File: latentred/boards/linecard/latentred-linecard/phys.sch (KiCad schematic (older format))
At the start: 0 parts

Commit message: Continued work on line card design. Now have PSU and all PHYs, still working on clock distribution.
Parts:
- added C100, C101, C105, C106, C107, C108, C109, C110, C111, C112, C113, C117, C118, C119, C123, C124, C125, C145, C149, C153, C157, C16, C161, C162, C163, C164, C177, C178, C179, C180, C185, C186, C187, C188, C189, C190, C191, C192, C193, C194, C195, C196, C20, C201, C202, C203, C204, C205, C206, C207, C208, C209, C210, C211, C212, C217, C218, C219, C220, C225, C226, C227, C228, C233, C24, C25, C26, C27, C28, C29, C30, C31, C32, C63, C67, C71, C75, C76, C77, C87, C88, C89, C93, C94, C95, C96, C97, C98, C99: 0.47 uF, symbol device:C
- added C102, C103, C104, C114, C115, C116, C12, C120, C121, C122, C129, C13, C130, C131, C132, C133, C134, C135, C136, C137, C138, C139, C14, C140, C141, C142, C143, C144, C15, C181, C182, C183, C184, C197, C198, C199, C200, C213, C214, C215, C216, C221, C222, C223, C224, C46, C47, C48, C49, C51, C52, C53, C54, C55, C56, C57, C58, C59, C60, C61, C62, C90, C91, C92: 0.1 uF, symbol device:C
- added C126, C127, C128, C229, C230, C231, C232, C50: 10 nF 2 kV, symbol device:C
- added C146, C147, C148, C150, C151, C152, C154, C155, C156, C158, C159, C160, C165, C166, C167, C168, C169, C17, C170, C171, C172, C173, C174, C175, C176, C18, C19, C21, C22, C23, C64, C65, C66, C68, C69, C70, C72, C73, C74, C78, C79, C80, C81, C82, C83, C84, C85, C86: 4.7 uF, symbol device:C
- added J2: STEWART_SS_74500_024, symbol special-azonenberg:STEWART_SS_74500_024
- added L10, L11, L12, L13, L14, L15, L16, L20, L21, L22, L23, L24, L25, L26, L27, L28, L29, L30, L31, L4, L5, L6, L8, L9: 600R, symbol passive-azonenberg:INDUCTOR_PWROUT
- added L17, L18, L19, L32, L33, L34, L35, L7: BOURNS_PT6120EL, symbol special-azonenberg:BOURNS_PT6120EL
- added Q1, Q2, Q3, Q4, Q5, Q6, Q7, Q8: SSM6N58NU, symbol special-azonenberg:SSM6N58NU_DUAL_NMOS
- added R100, R101, R102, R103, R104, R105, R106, R107, R108, R109, R110, R132, R134, R136, R138, R23, R26, R44, R45, R46, R47, R48, R49, R66, R68, R70, R94, R97, R98, R99: 2.49K, symbol device:R
- added R111, R112, R113, R114, R115, R116, R117, R118, R119, R121, R123, R125, R127, R128, R129, R130, R29, R30, R31, R32, R50, R51, R52, R53, R54, R55, R56, R58, R60, R62, R63, R64: 75, symbol device:R
- added R120, R122, R124, R126, R139, R140, R141, R142, R24, R27, R57, R59, R61, R71, R72, R73: 470, symbol device:R
- added R131, R133, R135, R137, R25, R40, R65, R67, R69, R86: 10K, symbol device:R
- added R143: 33, symbol device:R
- added R20, R33, R35, R37, R74, R76, R78, R80: 11K, symbol device:R
- added R21, R34, R36, R38, R75, R77, R79, R81, R83, R84, R87, R88, R91, R92, R95, R96: 10k, symbol device:R
- added R22, R39, R41, R43, R82, R85, R89, R93: 5.76K, symbol device:R
- added R28: 2.0K, symbol device:R
- added R42, R90: 5.76k, symbol device:R
- added U10, U11, U12, U13, U14, U15, U8, U9: DP83867, symbol special-azonenberg:DP83867
- added U16: DSC6101CI2A-025.0000, symbol osc-azonenberg:OSC
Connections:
- new net: R20.2, U8.12 (RBIAS)
- new net: C12.1, U8.27 (TX_D1/SGMII_TX_P)
- new net: C13.1, U8.28 (TX_D0/SGMII_TX_N)
- new net: C14.1, U8.35 (RX_D2/SGMII_RX_P)
- new net: C15.1, U8.36 (RX_D3/SGMII_RX_N)
- new net: R21.2, U8.44 (~INT~/~PWRDN~)
- new net: Q1.D1 (D), R24.2
- new net: Q1.D2 (D), R27.2
- new net: C49.2, L7.1 (A_CT)
- new net: C46.2, L7.10 (D_CT)
- new net: L7.15 (DM_CT), R32.2
- new net: L7.18 (CM_CT), R31.2
- new net: L7.21 (BM_CT), R30.2
- new net: L7.24 (AM_CT), R29.2
- new net: C48.2, L7.4 (B_CT)
- new net: C47.2, L7.7 (C_CT)
- new net: C50.2, R29.1, R30.1, R31.1, R32.1
- new net: R33.2, U9.12 (RBIAS)
- new net: C51.1, U9.27 (TX_D1/SGMII_TX_P)
- new net: C52.1, U9.28 (TX_D0/SGMII_TX_N)
- new net: C53.1, U9.35 (RX_D2/SGMII_RX_P)
- new net: C54.1, U9.36 (RX_D3/SGMII_RX_N)
- new net: R34.2, U9.44 (~INT~/~PWRDN~)
- new net: Q2.D1 (D), R57.2
- new net: Q3.D2 (D), R71.2
- new net: C120.2, L17.1 (A_CT)
- new net: C90.2, L17.10 (D_CT)
- new net: L17.15 (DM_CT), R62.2
- new net: L17.18 (CM_CT), R56.2
- new net: L17.21 (BM_CT), R53.2
- new net: L17.24 (AM_CT), R50.2
- new net: C114.2, L17.4 (B_CT)
- new net: C102.2, L17.7 (C_CT)
- new net: C126.2, R50.1, R53.1, R56.1, R62.1
- new net: R35.2, U10.12 (RBIAS)
- new net: C55.1, U10.27 (TX_D1/SGMII_TX_P)
- new net: C56.1, U10.28 (TX_D0/SGMII_TX_N)
- new net: C57.1, U10.35 (RX_D2/SGMII_RX_P)
- new net: C58.1, U10.36 (RX_D3/SGMII_RX_N)
- new net: R36.2, U10.44 (~INT~/~PWRDN~)
- new net: Q2.D2 (D), R59.2
- new net: Q4.D1 (D), R72.2
- new net: C121.2, L18.1 (A_CT)
- new net: C91.2, L18.10 (D_CT)
- new net: L18.15 (DM_CT), R63.2
- new net: L18.18 (CM_CT), R58.2
- new net: L18.21 (BM_CT), R54.2
- new net: L18.24 (AM_CT), R51.2
- new net: C115.2, L18.4 (B_CT)
- new net: C103.2, L18.7 (C_CT)
- new net: C127.2, R51.1, R54.1, R58.1, R63.1
- new net: R37.2, U11.12 (RBIAS)
- new net: C59.1, U11.27 (TX_D1/SGMII_TX_P)
- new net: C60.1, U11.28 (TX_D0/SGMII_TX_N)
- new net: C61.1, U11.35 (RX_D2/SGMII_RX_P)
- new net: C62.1, U11.36 (RX_D3/SGMII_RX_N)
- new net: R38.2, U11.44 (~INT~/~PWRDN~)
- new net: Q3.D1 (D), R61.2
- new net: Q4.D2 (D), R73.2
- new net: C122.2, L19.1 (A_CT)
- new net: C92.2, L19.10 (D_CT)
- new net: L19.15 (DM_CT), R64.2
- new net: L19.18 (CM_CT), R60.2
- new net: L19.21 (BM_CT), R55.2
- new net: L19.24 (AM_CT), R52.2
- new net: C116.2, L19.4 (B_CT)
- new net: C104.2, L19.7 (C_CT)
- new net: C128.2, R52.1, R55.1, R60.1, R64.1
- new net: R74.2, U12.12 (RBIAS)
- new net: C129.1, U12.27 (TX_D1/SGMII_TX_P)
- new net: C130.1, U12.28 (TX_D0/SGMII_TX_N)
- new net: R75.2, U12.44 (~INT~/~PWRDN~)
- new net: Q5.D1 (D), R120.2
- new net: Q7.D1 (D), R139.2
- new net: C221.2, L32.1 (A_CT)
- new net: C181.2, L32.10 (D_CT)
- new net: L32.15 (DM_CT), R127.2
- new net: L32.18 (CM_CT), R119.2
- new net: L32.21 (BM_CT), R115.2
- new net: L32.24 (AM_CT), R111.2
- new net: C213.2, L32.4 (B_CT)
- new net: C197.2, L32.7 (C_CT)
- new net: C229.2, R111.1, R115.1, R119.1, R127.1
- new net: R76.2, U13.12 (RBIAS)
- new net: C133.1, U13.27 (TX_D1/SGMII_TX_P)
- new net: C134.1, U13.28 (TX_D0/SGMII_TX_N)
- new net: R77.2, U13.44 (~INT~/~PWRDN~)
- new net: Q5.D2 (D), R122.2
- new net: Q7.D2 (D), R140.2
- new net: C222.2, L33.1 (A_CT)
- new net: C182.2, L33.10 (D_CT)
- new net: L33.15 (DM_CT), R128.2
- new net: L33.18 (CM_CT), R121.2
- new net: L33.21 (BM_CT), R116.2
- new net: L33.24 (AM_CT), R112.2
- new net: C214.2, L33.4 (B_CT)
- new net: C198.2, L33.7 (C_CT)
- new net: C230.2, R112.1, R116.1, R121.1, R128.1
- new net: R78.2, U14.12 (RBIAS)
- new net: C137.1, U14.27 (TX_D1/SGMII_TX_P)
- new net: C138.1, U14.28 (TX_D0/SGMII_TX_N)
- new net: R79.2, U14.44 (~INT~/~PWRDN~)
- new net: Q6.D1 (D), R124.2
- new net: Q8.D1 (D), R141.2
- new net: C223.2, L34.1 (A_CT)
- new net: C183.2, L34.10 (D_CT)
- new net: L34.15 (DM_CT), R129.2
- new net: L34.18 (CM_CT), R123.2
- new net: L34.21 (BM_CT), R117.2
- new net: L34.24 (AM_CT), R113.2
- new net: C215.2, L34.4 (B_CT)
- new net: C199.2, L34.7 (C_CT)
- new net: C231.2, R113.1, R117.1, R123.1, R129.1
- new net: R80.2, U15.12 (RBIAS)
- new net: C141.1, U15.27 (TX_D1/SGMII_TX_P)
- new net: C142.1, U15.28 (TX_D0/SGMII_TX_N)
- new net: R81.2, U15.44 (~INT~/~PWRDN~)
- new net: Q6.D2 (D), R126.2
- new net: Q8.D2 (D), R142.2
- new net: C224.2, L35.1 (A_CT)
- new net: C184.2, L35.10 (D_CT)
- new net: L35.15 (DM_CT), R130.2
- new net: L35.18 (CM_CT), R125.2
- new net: L35.21 (BM_CT), R118.2
- new net: L35.24 (AM_CT), R114.2
- new net: C216.2, L35.4 (B_CT)
- new net: C200.2, L35.7 (C_CT)
- new net: C232.2, R114.1, R118.1, R125.1, R130.1
- new net: R143.2, U16.3 (CLK)
- new net 1V0: C148.1, C152.1, C156.1, C160.1, C19.1, C66.1, C70.1, C74.1, L10.2, L13.2, L16.2, L22.2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
- new net 1V8: C145.1, C147.1, C149.1, C151.1, C153.1, C155.1, C157.1, C159.1, C16.1, C161.1, C162.1, C163.1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
- new net 2V5: C146.1, C150.1, C154.1, C158.1, C17.1, C64.1, C68.1, C72.1, L11.2, L14.2, L20.2, L23.2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
- new net 3V3: J2.A11 (YELLOW_LED_P), J2.A9 (GREEN_LED_P), J2.B11 (YELLOW_LED_P), J2.B9 (GREEN_LED_P), J2.C11 (YELLOW_LED_P), J2.C9 (GREEN_LED_P), J2.D11 (YELLOW_LED_P), J2.D9 (GREEN_LED_P), J2.E11 (YELLOW_LED_P), J2.E9 (GREEN_LED_P), J2.F11 (YELLOW_LED_P), J2.F9 (GREEN_LED_P)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
- new net A1V0_0: C23.1, C27.1, C30.1, C31.1, C32.1, L6.1, U8.24 (1V0), U8.31 (1V0), U8.42 (1V0), U8.6 (1V0)
- new net A1V0_1: C107.1, C117.1, C123.1, C80.1, C95.1, L10.1, U9.24 (1V0), U9.31 (1V0), U9.42 (1V0), U9.6 (1V0)
- new net A1V0_2: C110.1, C118.1, C124.1, C83.1, C98.1, L13.1, U10.24 (1V0), U10.31 (1V0), U10.42 (1V0), U10.6 (1V0)
- new net A1V0_3: C101.1, C113.1, C119.1, C125.1, C86.1, L16.1, U11.24 (1V0), U11.31 (1V0), U11.42 (1V0), U11.6 (1V0)
- new net A1V0_4: C167.1, C187.1, C203.1, C217.1, C225.1, L22.1, U12.24 (1V0), U12.31 (1V0), U12.42 (1V0), U12.6 (1V0)
- new net A1V0_5: C170.1, C190.1, C206.1, C218.1, C226.1, L25.1, U13.24 (1V0), U13.31 (1V0), U13.42 (1V0), U13.6 (1V0)
- new net A1V0_6: C173.1, C193.1, C209.1, C219.1, C227.1, L28.1, U14.24 (1V0), U14.31 (1V0), U14.42 (1V0), U14.6 (1V0)
- new net A1V0_7: C176.1, C196.1, C212.1, C220.1, C228.1, L31.1, U15.24 (1V0), U15.31 (1V0), U15.42 (1V0), U15.6 (1V0)
- new net A1V8_0: C22.1, C26.1, C29.1, L5.1, U8.13 (A1V8), U8.48 (A1V8)
- new net A1V8_1: C106.1, C79.1, C94.1, L9.1, U9.13 (A1V8), U9.48 (A1V8)
- new net A1V8_2: C109.1, C82.1, C97.1, L12.1, U10.13 (A1V8), U10.48 (A1V8)
- new net A1V8_3: C100.1, C112.1, C85.1, L15.1, U11.13 (A1V8), U11.48 (A1V8)
- new net A1V8_4: C166.1, C186.1, C202.1, L21.1, U12.13 (A1V8), U12.48 (A1V8)
- new net A1V8_5: C169.1, C189.1, C205.1, L24.1, U13.13 (A1V8), U13.48 (A1V8)
- new net A1V8_6: C172.1, C192.1, C208.1, L27.1, U14.13 (A1V8), U14.48 (A1V8)
- new net A1V8_7: C175.1, C195.1, C211.1, L30.1, U15.13 (A1V8), U15.48 (A1V8)
- new net A2V5_0: C21.1, C25.1, C28.1, L4.1, U8.3 (A2V5), U8.9 (A2V5)
- new net A2V5_1: C105.1, C78.1, C93.1, L8.1, U9.3 (A2V5), U9.9 (A2V5)
- new net A2V5_2: C108.1, C81.1, C96.1, L11.1, U10.3 (A2V5), U10.9 (A2V5)
- new net A2V5_3: C111.1, C84.1, C99.1, L14.1, U11.3 (A2V5), U11.9 (A2V5)
- new net A2V5_4: C165.1, C185.1, C201.1, L20.1, U12.3 (A2V5), U12.9 (A2V5)
- new net A2V5_5: C168.1, C188.1, C204.1, L23.1, U13.3 (A2V5), U13.9 (A2V5)
- new net A2V5_6: C171.1, C191.1, C207.1, L26.1, U14.3 (A2V5), U14.9 (A2V5)
- new net A2V5_7: C174.1, C194.1, C210.1, L29.1, U15.3 (A2V5), U15.9 (A2V5)
- new net CLK_25MHZ: R143.1
- new net CLK_25MHZ_0: U8.15 (XI)
- new net CLK_25MHZ_1: U9.15 (XI)
- new net CLK_25MHZ_2: U10.15 (XI)
- new net CLK_25MHZ_3: U11.15 (XI)
- new net CLK_25MHZ_4: U12.15 (XI)
- new net CLK_25MHZ_5: U13.15 (XI)
- new net CLK_25MHZ_6: U14.15 (XI)
- new net CLK_25MHZ_7: U15.15 (XI)
- new net ETH0_AM_N: J2.A2 (A_N), L7.22 (AM_N)
- new net ETH0_AM_P: J2.A1 (A_P), L7.23 (AM_P)
- new net ETH0_A_N: L7.3 (A_N), U8.2 (ETH_A_N)
- new net ETH0_A_P: L7.2 (A_P), U8.1 (ETH_A_P)
- new net ETH0_BM_N: J2.A4 (B_N), L7.19 (BM_N)
- new net ETH0_BM_P: J2.A3 (B_P), L7.20 (BM_P)
- new net ETH0_B_N: L7.6 (B_N), U8.5 (ETH_B_N)
- new net ETH0_B_P: L7.5 (B_P), U8.4 (ETH_B_P)
- new net ETH0_CM_N: J2.A6 (C_N), L7.16 (CM_N)
- new net ETH0_CM_P: J2.A5 (C_P), L7.17 (CM_P)
- new net ETH0_C_N: L7.9 (C_N), U8.8 (ETH_C_N)
- new net ETH0_C_P: L7.8 (C_P), U8.7 (ETH_C_P)
- new net ETH0_DM_N: J2.A8 (D_N), L7.13 (DM_N)
- new net ETH0_DM_P: J2.A7 (D_P), L7.14 (DM_P)
- new net ETH0_D_N: L7.12 (D_N), U8.11 (ETH_D_N)
- new net ETH0_D_P: L7.11 (D_P), U8.10 (ETH_D_P)
- new net ETH1_AM_N: J2.B2 (A_N), L17.22 (AM_N)
- new net ETH1_AM_P: J2.B1 (A_P), L17.23 (AM_P)
- new net ETH1_A_N: L17.3 (A_N), U9.2 (ETH_A_N)
- new net ETH1_A_P: L17.2 (A_P), U9.1 (ETH_A_P)
- new net ETH1_BM_N: J2.B4 (B_N), L17.19 (BM_N)
- new net ETH1_BM_P: J2.B3 (B_P), L17.20 (BM_P)
- new net ETH1_B_N: L17.6 (B_N), U9.5 (ETH_B_N)
- new net ETH1_B_P: L17.5 (B_P), U9.4 (ETH_B_P)
- new net ETH1_CM_N: J2.B6 (C_N), L17.16 (CM_N)
- new net ETH1_CM_P: J2.B5 (C_P), L17.17 (CM_P)
- new net ETH1_C_N: L17.9 (C_N), U9.8 (ETH_C_N)
- new net ETH1_C_P: L17.8 (C_P), U9.7 (ETH_C_P)
- new net ETH1_DM_N: J2.B8 (D_N), L17.13 (DM_N)
- new net ETH1_DM_P: J2.B7 (D_P), L17.14 (DM_P)
- new net ETH1_D_N: L17.12 (D_N), U9.11 (ETH_D_N)
- new net ETH1_D_P: L17.11 (D_P), U9.10 (ETH_D_P)
- new net ETH2_AM_N: J2.C2 (A_N), L18.22 (AM_N)
- new net ETH2_AM_P: J2.C1 (A_P), L18.23 (AM_P)
- new net ETH2_A_N: L18.3 (A_N), U10.2 (ETH_A_N)
- new net ETH2_A_P: L18.2 (A_P), U10.1 (ETH_A_P)
- new net ETH2_BM_N: J2.C4 (B_N), L18.19 (BM_N)
- new net ETH2_BM_P: J2.C3 (B_P), L18.20 (BM_P)
- new net ETH2_B_N: L18.6 (B_N), U10.5 (ETH_B_N)
- new net ETH2_B_P: L18.5 (B_P), U10.4 (ETH_B_P)
- new net ETH2_CM_N: J2.C6 (C_N), L18.16 (CM_N)
- new net ETH2_CM_P: J2.C5 (C_P), L18.17 (CM_P)
- new net ETH2_C_N: L18.9 (C_N), U10.8 (ETH_C_N)
- new net ETH2_C_P: L18.8 (C_P), U10.7 (ETH_C_P)
- new net ETH2_DM_N: J2.C8 (D_N), L18.13 (DM_N)
- new net ETH2_DM_P: J2.C7 (D_P), L18.14 (DM_P)
- new net ETH2_D_N: L18.12 (D_N), U10.11 (ETH_D_N)
- new net ETH2_D_P: L18.11 (D_P), U10.10 (ETH_D_P)
- new net ETH3_AM_N: J2.D2 (A_N), L19.22 (AM_N)
- new net ETH3_AM_P: J2.D1 (A_P), L19.23 (AM_P)
- new net ETH3_A_N: L19.3 (A_N), U11.2 (ETH_A_N)
- new net ETH3_A_P: L19.2 (A_P), U11.1 (ETH_A_P)
- new net ETH3_BM_N: J2.D4 (B_N), L19.19 (BM_N)
- new net ETH3_BM_P: J2.D3 (B_P), L19.20 (BM_P)
- new net ETH3_B_N: L19.6 (B_N), U11.5 (ETH_B_N)
- new net ETH3_B_P: L19.5 (B_P), U11.4 (ETH_B_P)
- new net ETH3_CM_N: J2.D6 (C_N), L19.16 (CM_N)
- new net ETH3_CM_P: J2.D5 (C_P), L19.17 (CM_P)
- new net ETH3_C_N: L19.9 (C_N), U11.8 (ETH_C_N)
- new net ETH3_C_P: L19.8 (C_P), U11.7 (ETH_C_P)
- new net ETH3_DM_N: J2.D8 (D_N), L19.13 (DM_N)
- new net ETH3_DM_P: J2.D7 (D_P), L19.14 (DM_P)
- new net ETH3_D_N: L19.12 (D_N), U11.11 (ETH_D_N)
- new net ETH3_D_P: L19.11 (D_P), U11.10 (ETH_D_P)
- new net ETH4_AM_N: J2.E2 (A_N), L32.22 (AM_N)
- new net ETH4_AM_P: J2.E1 (A_P), L32.23 (AM_P)
- new net ETH4_A_N: L32.3 (A_N), U12.2 (ETH_A_N)
- new net ETH4_A_P: L32.2 (A_P), U12.1 (ETH_A_P)
- new net ETH4_BM_N: J2.E4 (B_N), L32.19 (BM_N)
- new net ETH4_BM_P: J2.E3 (B_P), L32.20 (BM_P)
- new net ETH4_B_N: L32.6 (B_N), U12.5 (ETH_B_N)
- new net ETH4_B_P: L32.5 (B_P), U12.4 (ETH_B_P)
- new net ETH4_CM_N: J2.E6 (C_N), L32.16 (CM_N)
- new net ETH4_CM_P: J2.E5 (C_P), L32.17 (CM_P)
- new net ETH4_C_N: L32.9 (C_N), U12.8 (ETH_C_N)
- new net ETH4_C_P: L32.8 (C_P), U12.7 (ETH_C_P)
- new net ETH4_DM_N: J2.E8 (D_N), L32.13 (DM_N)
- new net ETH4_DM_P: J2.E7 (D_P), L32.14 (DM_P)
- new net ETH4_D_N: L32.12 (D_N), U12.11 (ETH_D_N)
- new net ETH4_D_P: L32.11 (D_P), U12.10 (ETH_D_P)
- new net ETH5_AM_N: J2.F2 (A_N), L33.22 (AM_N)
- new net ETH5_AM_P: J2.F1 (A_P), L33.23 (AM_P)
- new net ETH5_A_N: L33.3 (A_N), U13.2 (ETH_A_N)
- new net ETH5_A_P: L33.2 (A_P), U13.1 (ETH_A_P)
- new net ETH5_BM_N: J2.F4 (B_N), L33.19 (BM_N)
- new net ETH5_BM_P: J2.F3 (B_P), L33.20 (BM_P)
- new net ETH5_B_N: L33.6 (B_N), U13.5 (ETH_B_N)
- new net ETH5_B_P: L33.5 (B_P), U13.4 (ETH_B_P)
- new net ETH5_CM_N: J2.F6 (C_N), L33.16 (CM_N)
- new net ETH5_CM_P: J2.F5 (C_P), L33.17 (CM_P)
- new net ETH5_C_N: L33.9 (C_N), U13.8 (ETH_C_N)
- new net ETH5_C_P: L33.8 (C_P), U13.7 (ETH_C_P)
- new net ETH5_DM_N: J2.F8 (D_N), L33.13 (DM_N)
- new net ETH5_DM_P: J2.F7 (D_P), L33.14 (DM_P)
- new net ETH5_D_N: L33.12 (D_N), U13.11 (ETH_D_N)
- new net ETH5_D_P: L33.11 (D_P), U13.10 (ETH_D_P)
- new net ETH6_AM_N: J2.G2 (A_N), L34.22 (AM_N)
- new net ETH6_AM_P: J2.G1 (A_P), L34.23 (AM_P)
- new net ETH6_A_N: L34.3 (A_N), U14.2 (ETH_A_N)
- new net ETH6_A_P: L34.2 (A_P), U14.1 (ETH_A_P)
- new net ETH6_BM_N: J2.G4 (B_N), L34.19 (BM_N)
- new net ETH6_BM_P: J2.G3 (B_P), L34.20 (BM_P)
- new net ETH6_B_N: L34.6 (B_N), U14.5 (ETH_B_N)
- new net ETH6_B_P: L34.5 (B_P), U14.4 (ETH_B_P)
- new net ETH6_CM_N: J2.G6 (C_N), L34.16 (CM_N)
- new net ETH6_CM_P: J2.G5 (C_P), L34.17 (CM_P)
- new net ETH6_C_N: L34.9 (C_N), U14.8 (ETH_C_N)
- new net ETH6_C_P: L34.8 (C_P), U14.7 (ETH_C_P)
- new net ETH6_DM_N: J2.G8 (D_N), L34.13 (DM_N)
- new net ETH6_DM_P: J2.G7 (D_P), L34.14 (DM_P)
- new net ETH6_D_N: L34.12 (D_N), U14.11 (ETH_D_N)
- new net ETH6_D_P: L34.11 (D_P), U14.10 (ETH_D_P)
- new net ETH7_AM_N: J2.H2 (A_N), L35.22 (AM_N)
- new net ETH7_AM_P: J2.H1 (A_P), L35.23 (AM_P)
- new net ETH7_A_N: L35.3 (A_N), U15.2 (ETH_A_N)
- new net ETH7_A_P: L35.2 (A_P), U15.1 (ETH_A_P)
- new net ETH7_BM_N: J2.H4 (B_N), L35.19 (BM_N)
- new net ETH7_BM_P: J2.H3 (B_P), L35.20 (BM_P)
- new net ETH7_B_N: L35.6 (B_N), U15.5 (ETH_B_N)
- new net ETH7_B_P: L35.5 (B_P), U15.4 (ETH_B_P)
- new net ETH7_CM_N: J2.H6 (C_N), L35.16 (CM_N)
- new net ETH7_CM_P: J2.H5 (C_P), L35.17 (CM_P)
- new net ETH7_C_N: L35.9 (C_N), U15.8 (ETH_C_N)
- new net ETH7_C_P: L35.8 (C_P), U15.7 (ETH_C_P)
- new net ETH7_DM_N: J2.H8 (D_N), L35.13 (DM_N)
- new net ETH7_DM_P: J2.H7 (D_P), L35.14 (DM_P)
- new net ETH7_D_N: L35.12 (D_N), U15.11 (ETH_D_N)
- new net ETH7_D_P: L35.11 (D_P), U15.10 (ETH_D_P)
- new net GND: C100.2, C101.2, C102.1, C103.1, C104.1, C105.2, C106.2, C107.2, C108.2, C109.2, C110.2, C111.2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
- new net JTAG_TCK: U10.20 (JTAG_TCK), U11.20 (JTAG_TCK), U12.20 (JTAG_TCK), U13.20 (JTAG_TCK), U14.20 (JTAG_TCK), U15.20 (JTAG_TCK), U8.20 (JTAG_TCK), U9.20 (JTAG_TCK)
- new net JTAG_TDI: U8.23 (JTAG_TDI)
- new net JTAG_TDO: U15.21 (JTAG_TDO)
- new net JTAG_TDO_0: U8.21 (JTAG_TDO), U9.23 (JTAG_TDI)
- new net JTAG_TDO_1: U10.23 (JTAG_TDI), U9.21 (JTAG_TDO)
- new net JTAG_TDO_2: U10.21 (JTAG_TDO), U11.23 (JTAG_TDI)
- new net JTAG_TDO_3: U11.21 (JTAG_TDO), U12.23 (JTAG_TDI)
- new net JTAG_TDO_4: U12.21 (JTAG_TDO), U13.23 (JTAG_TDI)
- new net JTAG_TDO_5: U13.21 (JTAG_TDO), U14.23 (JTAG_TDI)
- new net JTAG_TDO_6: U14.21 (JTAG_TDO), U15.23 (JTAG_TDI)
- new net JTAG_TMS: U10.22 (JTAG_TMS), U11.22 (JTAG_TMS), U12.22 (JTAG_TMS), U13.22 (JTAG_TMS), U14.22 (JTAG_TMS), U15.22 (JTAG_TMS), U8.22 (JTAG_TMS), U9.22 (JTAG_TMS)
- new net LED0_0_N: J2.A10 (GREEN_LED_N), R27.1
- new net LED0_1_N: J2.B10 (GREEN_LED_N), R71.1
- new net LED0_2_N: J2.C10 (GREEN_LED_N), J2.D10 (GREEN_LED_N), R72.1
- new net LED0_3_N: R73.1
- new net LED0_4_N: J2.E10 (GREEN_LED_N), R139.1
- new net LED0_5_N: J2.F10 (GREEN_LED_N), R140.1
- new net LED0_6_N: J2.G10 (GREEN_LED_N), R141.1
- new net LED0_7_N: J2.H10 (GREEN_LED_N), R142.1
- new net LED1_0_N: J2.A12 (YELLOW_LED_N), R24.1
- new net LED1_1_N: J2.B12 (YELLOW_LED_N), R57.1
- new net LED1_2_N: J2.C12 (YELLOW_LED_N), J2.D12 (YELLOW_LED_N), R59.1
- new net LED1_3_N: R61.1
- new net LED1_4_N: J2.E12 (YELLOW_LED_N), R120.1
- new net LED1_5_N: J2.F12 (YELLOW_LED_N), R122.1
- new net LED1_6_N: J2.G12 (YELLOW_LED_N), R124.1
- new net LED1_7_N: J2.H12 (YELLOW_LED_N), R126.1
- new net LED_0_0: Q1.G2 (G), R25.2, R26.1, U8.47 (LED_0)
- new net LED_0_1: Q3.G2 (G), R65.2, R66.1, U9.47 (LED_0)
- new net LED_0_2: Q4.G1 (G), R67.2, R68.1, U10.47 (LED_0)
- new net LED_0_3: Q4.G2 (G), R69.2, R70.1, U11.47 (LED_0)
- new net LED_0_4: Q7.G1 (G), R131.2, R132.1, U12.47 (LED_0)
- new net LED_0_5: Q7.G2 (G), R133.2, R134.1, U13.47 (LED_0)
- new net LED_0_6: Q8.G1 (G), R135.2, R136.1, U14.47 (LED_0)
- new net LED_0_7: Q8.G2 (G), R137.2, R138.1, U15.47 (LED_0)
- new net LED_1_0: Q1.G1 (G), U8.46 (LED_1)
- new net LED_1_1: Q2.G1 (G), U9.46 (LED_1)
- new net LED_1_2: Q2.G2 (G), U10.46 (LED_1)
- new net LED_1_3: Q3.G1 (G), U11.46 (LED_1)
- new net LED_1_4: Q5.G1 (G), U12.46 (LED_1)
- new net LED_1_5: Q5.G2 (G), U13.46 (LED_1)
- new net LED_1_6: Q6.G1 (G), U14.46 (LED_1)
- new net LED_1_7: Q6.G2 (G), U15.46 (LED_1)
- new net MGMT_MDC: U10.16 (MDC), U11.16 (MDC), U12.16 (MDC), U13.16 (MDC), U14.16 (MDC), U15.16 (MDC), U8.16 (MDC), U9.16 (MDC)
- new net MGMT_MDIO: R28.2, U10.17 (MDIO), U11.17 (MDIO), U12.17 (MDIO), U13.17 (MDIO), U14.17 (MDIO), U15.17 (MDIO), U8.17 (MDIO), U9.17 (MDIO)
- new net PHY_RST_N: U10.43 (~RESET), U11.43 (~RESET), U12.43 (~RESET), U13.43 (~RESET), U14.43 (~RESET), U15.43 (~RESET), U8.43 (~RESET), U9.43 (~RESET)
- new net RX_CTRL_0: R22.1, R23.2, U8.38 (RX_CTRL)
- new net RX_CTRL_1: R39.1, R45.2, U11.38 (RX_CTRL), U9.38 (RX_CTRL)
- new net RX_CTRL_2: R104.2, R41.1, R47.2, R89.1, U10.38 (RX_CTRL)
- new net RX_CTRL_3: R43.1, R49.2
- new net RX_CTRL_4: R82.1, R97.2, U12.38 (RX_CTRL)
- new net RX_CTRL_5: R100.2, R85.1, U13.38 (RX_CTRL)
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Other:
- note added: "PHY 0 strap config:\n* RX_D0 / PHY_ADD[1:0]: mode 1 (2'b00)\n* RX_D2 / PHY_ADD[3:2]: mode 1 (2'b00)\n* RX_D3: not a strap but needs to be balanced with RX_D2 (mode 0)\n* RX_CTRL / ANEG_DISABLE: mode 3 (not disabled)\n* GPIO_0 / RGMII_RX_SKEW[0]: mode 1 (0)\n* GPIO_1 / RGMII_RX_SKEW[2:1]: mode 1 (0)\n* LED_2 / RGMII_TX_SKEW[1:0]: mode 1 (0)\n* LED_1 / ANEG_SEL, RGMII_TX_SKEW[2]: mode 1 (0, 0)\n* L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"
- note added: "PHY 1 strap config:\n* RX_D0 / PHY_ADD[1:0]: mode 2 (2'b01)\n* RX_D2 / PHY_ADD[3:2]: mode 1 (2'b00)\n* RX_D3: not a strap but needs to be balanced with RX_D2 (mode 0)\n* RX_CTRL / ANEG_DISABLE: mode 3 (not disabled)\n* GPIO_0 / RGMII_RX_SKEW[0]: mode 1 (0)\n* GPIO_1 / RGMII_RX_SKEW[2:1]: mode 1 (0)\n* LED_2 / RGMII_TX_SKEW[1:0]: mode 1 (0)\n* LED_1 / ANEG_SEL, RGMII_TX_SKEW[2]: mode 1 (0, 0)\n* L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"
- note added: "PHY 1 strap config:\n* RX_D0 / PHY_ADD[1:0]: mode 2 (2'b01)\n* RX_D2 / PHY_ADD[3:2]: mode 2 (2'b01)\n* RX_D3: not a strap but needs to be balanced with RX_D2 (mode 2)\n* RX_CTRL / ANEG_DISABLE: mode 3 (not disabled)\n* GPIO_0 / RGMII_RX_SKEW[0]: mode 1 (0)\n* GPIO_1 / RGMII_RX_SKEW[2:1]: mode 1 (0)\n* LED_2 / RGMII_TX_SKEW[1:0]: mode 1 (0)\n* LED_1 / ANEG_SEL, RGMII_TX_SKEW[2]: mode 1 (0, 0)\n* L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"
- note added: "PHY 2 strap config:\n* RX_D0 / PHY_ADD[1:0]: mode 3 (2'b10)\n* RX_D2 / PHY_ADD[3:2]: mode 1 (2'b00)\n* RX_D3: not a strap but needs to be balanced with RX_D2 (mode 0)\n* RX_CTRL / ANEG_DISABLE: mode 3 (not disabled)\n* GPIO_0 / RGMII_RX_SKEW[0]: mode 1 (0)\n* GPIO_1 / RGMII_RX_SKEW[2:1]: mode 1 (0)\n* LED_2 / RGMII_TX_SKEW[1:0]: mode 1 (0)\n* LED_1 / ANEG_SEL, RGMII_TX_SKEW[2]: mode 1 (0, 0)\n* L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"
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
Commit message: Finished initial version of LATENTRED line card schematic. Not yet reviewed.
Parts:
- added C234: 4.7 uF, symbol device:C
- added C235, C236, C237: 0.47 uF, symbol device:C
- added R144, R145, R146, R147, R148, R149, R150, R151: 33, symbol device:R
- added U17: 5PB1108CMG, symbol special-azonenberg:5PB1108CMG
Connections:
- net 1V8: now also C234.1, C235.1, C236.1, C237.1, U17.12 (VDD), U17.16 (OE), U17.3 (VDD), U17.8 (VDD)
- net CLK_25MHZ: now also U17.15 (CLKIN)
- net CLK_25MHZ_0: now also R144.1
- net CLK_25MHZ_1: now also R145.1
- net CLK_25MHZ_2: now also R146.1
- net CLK_25MHZ_3: now also R147.1
- net CLK_25MHZ_4: now also R148.1
- net CLK_25MHZ_5: now also R149.1
- net CLK_25MHZ_6: now also R150.1
- net CLK_25MHZ_7: now also R151.1
- net GND: now also C234.2, C235.2, C236.2, C237.2, U17.10 (GND), U17.2 (GND), U17.5 (GND)
- net LED0_2_N: no longer J2.D10 (GREEN_LED_N)
- net LED0_3_N: now also J2.D10 (GREEN_LED_N)
- net LED1_2_N: no longer J2.D12 (YELLOW_LED_N)
- net LED1_3_N: now also J2.D12 (YELLOW_LED_N)
- net RX_CTRL_1: no longer U11.38 (RX_CTRL)
- net RX_CTRL_2: no longer R104.2, R89.1
- net RX_CTRL_3: now also U11.38 (RX_CTRL)
- net RX_CTRL_6: now also R104.2, R89.1
- net RX_D0_2: no longer R105.2, R90.1
- net RX_D0_6: now also R105.2, R90.1
- new net: R144.2, U17.1 (CLKOUT0)
- new net: R149.2, U17.11 (CLKOUT5)
- new net: R150.2, U17.13 (CLKOUT6)
- new net: R151.2, U17.14 (CLKOUT7)
- new net: R145.2, U17.4 (CLKOUT1)
- new net: R146.2, U17.6 (CLKOUT2)
- new net: R147.2, U17.7 (CLKOUT3)
- new net: R148.2, U17.9 (CLKOUT4)
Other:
- note removed: "TODO: right side RX_D2 strap"

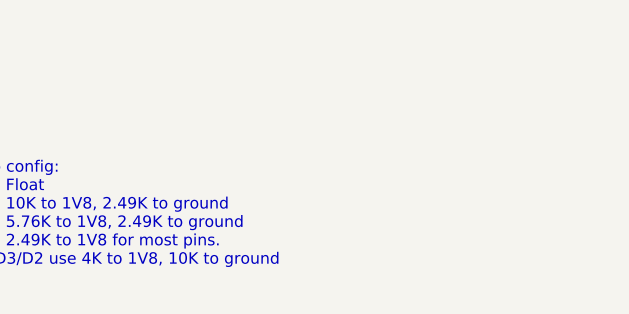
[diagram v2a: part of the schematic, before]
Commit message: Finished initial footprint creation, ready to begin layout
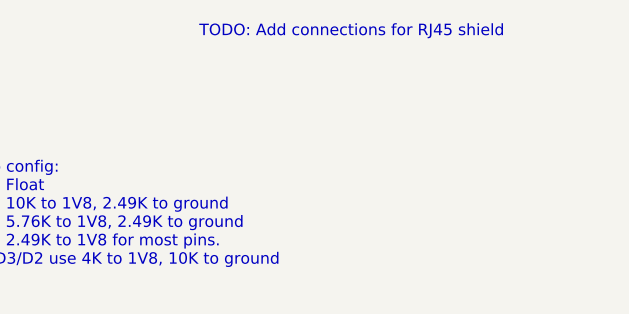
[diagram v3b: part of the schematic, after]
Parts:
- C100, C101, C102, C103, C104, C105, C106, C107, C108, C109, C110, C111, C112, C113, C114, C115, C116, C117, C118, C119, C12, C120, C121, C122, C123, C124, C125, C129, C13, C130, C131, C132, C133, C134, C135, C136, C137, C138, C139, C14, C140, C141, C142, C143, C144, C145, C149, C15, C153, C157, C16, C161, C162, C163, C164, C177, C178, C179, C180, C181, C182, C183, C184, C185, C186, C187, C188, C189, C190, C191, C192, C193, C194, C195, C196, C197, C198, C199, C20, C200, C201, C202, C203, C204, C205, C206, C207, C208, C209, C210, C211, C212, C213, C214, C215, C216, C217, C218, C219, C220, C221, C222, C223, C224, C225, C226, C227, C228, C233, C235, C236, C237, C24, C25, C26, C27, C28, C29, C30, C31, C32, C46, C47, C48, C49, C51, C52, C53, C54, C55, C56, C57, C58, C59, C60, C61, C62, C63, C67, C71, C75, C76, C77, C87, C88, C89, C90, C91, C92, C93, C94, C95, C96, C97, C98, C99: footprint (none) -> azonenberg_pcb:EIA_0402_CAP_NOSILK
- C126, C127, C128, C229, C230, C231, C232, C50: footprint (none) -> azonenberg_pcb:EIA_1812_CAP_NOSILK
- C146, C147, C148, C150, C151, C152, C154, C155, C156, C158, C159, C160, C165, C166, C167, C168, C169, C17, C170, C171, C172, C173, C174, C175, C176, C18, C19, C21, C22, C23, C234, C64, C65, C66, C68, C69, C70, C72, C73, C74, C78, C79, C80, C81, C82, C83, C84, C85, C86: footprint (none) -> azonenberg_pcb:EIA_0603_CAP_NOSILK
- J2: footprint (none) -> azonenberg_pcb:CONN_STEWART_SS_74500_024
- L10, L11, L12, L13, L14, L15, L16, L20, L21, L22, L23, L24, L25, L26, L27, L28, L29, L30, L31, L4, L5, L6, L8, L9, R100, R101, R102, R103, R104, R105, R106, R107, R108, R109, R110, R111, R112, R113, R114, R115, R116, R117, R118, R119, R120, R121, R122, R123, R124, R125, R126, R127, R128, R129, R130, R131, R132, R133, R134, R135, R136, R137, R138, R139, R140, R141, R142, R143, R144, R145, R146, R147, R148, R149, R150, R151, R20, R21, R22, R23, R24, R25, R26, R27, R28, R29, R30, R31, R32, R33, R34, R35, R36, R37, R38, R39, R40, R41, R42, R43, R44, R45, R46, R47, R48, R49, R50, R51, R52, R53, R54, R55, R56, R57, R58, R59, R60, R61, R62, R63, R64, R65, R66, R67, R68, R69, R70, R71, R72, R73, R74, R75, R76, R77, R78, R79, R80, R81, R82, R83, R84, R85, R86, R87, R88, R89, R90, R91, R92, R93, R94, R95, R96, R97, R98, R99: footprint (none) -> azonenberg_pcb:EIA_0402_RES_NOSILK
- L17, L18, L19, L32, L33, L34, L35, L7: footprint (none) -> azonenberg_pcb:BOURNS_PT61020EL
- Q1, Q2, Q3, Q4, Q5, Q6, Q7, Q8: footprint (none) -> azonenberg_pcb:DFN_6_0.65MM_2x2MM_GDS
- U10, U11, U12, U13, U14, U15, U8, U9: footprint (none) -> azonenberg_pcb:QFN_48_0.5MM_7x7MM
- U16: footprint (none) -> azonenberg_pcb:OSCILLATOR_3.2x2.5
- U17: footprint (none) -> azonenberg_pcb:QFN_16_0.4MM_2p5x2.5MM_NOPAD
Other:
- note added: "TODO: Add connections for RJ45 shield"

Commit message: Continued magnetic-and-RJ45 layout
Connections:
- net ETH0_AM_N: now also L7.13 (DM_N); no longer L7.22 (AM_N)
- net ETH0_AM_P: now also L7.14 (DM_P); no longer L7.23 (AM_P)
- net ETH0_A_N: now also L7.12 (D_N); no longer L7.3 (A_N)
- net ETH0_A_P: now also L7.11 (D_P); no longer L7.2 (A_P)
- net ETH0_BM_N: now also L7.16 (CM_N); no longer L7.19 (BM_N)
- net ETH0_BM_P: now also L7.17 (CM_P); no longer L7.20 (BM_P)
- net ETH0_B_N: now also L7.9 (C_N); no longer L7.6 (B_N)
- net ETH0_B_P: now also L7.8 (C_P); no longer L7.5 (B_P)
- net ETH0_CM_N: now also L7.19 (BM_N); no longer L7.16 (CM_N)
- net ETH0_CM_P: now also L7.20 (BM_P); no longer L7.17 (CM_P)
- net ETH0_C_N: now also L7.6 (B_N); no longer L7.9 (C_N)
- net ETH0_C_P: now also L7.5 (B_P); no longer L7.8 (C_P)
- net ETH0_DM_N: now also L7.22 (AM_N); no longer L7.13 (DM_N)
- net ETH0_DM_P: now also L7.23 (AM_P); no longer L7.14 (DM_P)
- net ETH0_D_N: now also L7.3 (A_N); no longer L7.12 (D_N)
- net ETH0_D_P: now also L7.2 (A_P); no longer L7.11 (D_P)
- net ETH1_AM_N: now also L17.13 (DM_N); no longer L17.22 (AM_N)
- net ETH1_AM_P: now also L17.14 (DM_P); no longer L17.23 (AM_P)
- net ETH1_A_N: now also L17.12 (D_N); no longer L17.3 (A_N)
- net ETH1_A_P: now also L17.11 (D_P); no longer L17.2 (A_P)
- net ETH1_BM_N: now also L17.16 (CM_N); no longer L17.19 (BM_N)
- net ETH1_BM_P: now also L17.17 (CM_P); no longer L17.20 (BM_P)
- net ETH1_B_N: now also L17.9 (C_N); no longer L17.6 (B_N)
- net ETH1_B_P: now also L17.8 (C_P); no longer L17.5 (B_P)
- net ETH1_CM_N: now also L17.19 (BM_N); no longer L17.16 (CM_N)
- net ETH1_CM_P: now also L17.20 (BM_P); no longer L17.17 (CM_P)
- net ETH1_C_N: now also L17.6 (B_N); no longer L17.9 (C_N)
- net ETH1_C_P: now also L17.5 (B_P); no longer L17.8 (C_P)
- net ETH1_DM_N: now also L17.22 (AM_N); no longer L17.13 (DM_N)
- net ETH1_DM_P: now also L17.23 (AM_P); no longer L17.14 (DM_P)
- net ETH1_D_N: now also L17.3 (A_N); no longer L17.12 (D_N)
- net ETH1_D_P: now also L17.2 (A_P); no longer L17.11 (D_P)
- net ETH2_AM_N: now also L18.13 (DM_N); no longer L18.22 (AM_N)
- net ETH2_AM_P: now also L18.14 (DM_P); no longer L18.23 (AM_P)
- net ETH2_A_N: now also L18.12 (D_N); no longer L18.3 (A_N)
- net ETH2_A_P: now also L18.11 (D_P); no longer L18.2 (A_P)
- net ETH2_BM_N: now also L18.16 (CM_N); no longer L18.19 (BM_N)
- net ETH2_BM_P: now also L18.17 (CM_P); no longer L18.20 (BM_P)
- net ETH2_B_N: now also L18.9 (C_N); no longer L18.6 (B_N)
- net ETH2_B_P: now also L18.8 (C_P); no longer L18.5 (B_P)
- net ETH2_CM_N: now also L18.19 (BM_N); no longer L18.16 (CM_N)
- net ETH2_CM_P: now also L18.20 (BM_P); no longer L18.17 (CM_P)
- net ETH2_C_N: now also L18.6 (B_N); no longer L18.9 (C_N)
- net ETH2_C_P: now also L18.5 (B_P); no longer L18.8 (C_P)
- net ETH2_DM_N: now also L18.22 (AM_N); no longer L18.13 (DM_N)
- net ETH2_DM_P: now also L18.23 (AM_P); no longer L18.14 (DM_P)
- net ETH2_D_N: now also L18.3 (A_N); no longer L18.12 (D_N)
- net ETH2_D_P: now also L18.2 (A_P); no longer L18.11 (D_P)
- net ETH3_AM_N: now also L19.13 (DM_N); no longer L19.22 (AM_N)
- net ETH3_AM_P: now also L19.14 (DM_P); no longer L19.23 (AM_P)
- net ETH3_A_N: now also L19.12 (D_N); no longer L19.3 (A_N)
- net ETH3_A_P: now also L19.11 (D_P); no longer L19.2 (A_P)
- net ETH3_BM_N: now also L19.16 (CM_N); no longer L19.19 (BM_N)
- net ETH3_BM_P: now also L19.17 (CM_P); no longer L19.20 (BM_P)
- net ETH3_B_N: now also L19.9 (C_N); no longer L19.6 (B_N)
- net ETH3_B_P: now also L19.8 (C_P); no longer L19.5 (B_P)
- net ETH3_CM_N: now also L19.19 (BM_N); no longer L19.16 (CM_N)
- net ETH3_CM_P: now also L19.20 (BM_P); no longer L19.17 (CM_P)
- net ETH3_C_N: now also L19.6 (B_N); no longer L19.9 (C_N)
- net ETH3_C_P: now also L19.5 (B_P); no longer L19.8 (C_P)
- net ETH3_DM_N: now also L19.22 (AM_N); no longer L19.13 (DM_N)
- net ETH3_DM_P: now also L19.23 (AM_P); no longer L19.14 (DM_P)
- net ETH3_D_N: now also L19.3 (A_N); no longer L19.12 (D_N)
- net ETH3_D_P: now also L19.2 (A_P); no longer L19.11 (D_P)
- net ETH4_AM_N: now also L32.13 (DM_N); no longer L32.22 (AM_N)
- net ETH4_AM_P: now also L32.14 (DM_P); no longer L32.23 (AM_P)
- net ETH4_A_N: now also L32.12 (D_N); no longer L32.3 (A_N)
- net ETH4_A_P: now also L32.11 (D_P); no longer L32.2 (A_P)
- net ETH4_BM_N: now also L32.16 (CM_N); no longer L32.19 (BM_N)
- net ETH4_BM_P: now also L32.17 (CM_P); no longer L32.20 (BM_P)
- net ETH4_B_N: now also L32.9 (C_N); no longer L32.6 (B_N)
- net ETH4_B_P: now also L32.8 (C_P); no longer L32.5 (B_P)
- net ETH4_CM_N: now also L32.19 (BM_N); no longer L32.16 (CM_N)
- net ETH4_CM_P: now also L32.20 (BM_P); no longer L32.17 (CM_P)
- net ETH4_C_N: now also L32.6 (B_N); no longer L32.9 (C_N)
- net ETH4_C_P: now also L32.5 (B_P); no longer L32.8 (C_P)
- net ETH4_DM_N: now also L32.22 (AM_N); no longer L32.13 (DM_N)
- net ETH4_DM_P: now also L32.23 (AM_P); no longer L32.14 (DM_P)
- net ETH4_D_N: now also L32.3 (A_N); no longer L32.12 (D_N)
- net ETH4_D_P: now also L32.2 (A_P); no longer L32.11 (D_P)
- net ETH5_AM_N: now also L33.13 (DM_N); no longer L33.22 (AM_N)
- net ETH5_AM_P: now also L33.14 (DM_P); no longer L33.23 (AM_P)
- net ETH5_A_N: now also L33.12 (D_N); no longer L33.3 (A_N)
- net ETH5_A_P: now also L33.11 (D_P); no longer L33.2 (A_P)
- net ETH5_BM_N: now also L33.16 (CM_N); no longer L33.19 (BM_N)
- net ETH5_BM_P: now also L33.17 (CM_P); no longer L33.20 (BM_P)
- net ETH5_B_N: now also L33.9 (C_N); no longer L33.6 (B_N)
- net ETH5_B_P: now also L33.8 (C_P); no longer L33.5 (B_P)
- net ETH5_CM_N: now also L33.19 (BM_N); no longer L33.16 (CM_N)
- net ETH5_CM_P: now also L33.20 (BM_P); no longer L33.17 (CM_P)
- net ETH5_C_N: now also L33.6 (B_N); no longer L33.9 (C_N)
- net ETH5_C_P: now also L33.5 (B_P); no longer L33.8 (C_P)
- net ETH5_DM_N: now also L33.22 (AM_N); no longer L33.13 (DM_N)
- net ETH5_DM_P: now also L33.23 (AM_P); no longer L33.14 (DM_P)
- net ETH5_D_N: now also L33.3 (A_N); no longer L33.12 (D_N)
- net ETH5_D_P: now also L33.2 (A_P); no longer L33.11 (D_P)
- net ETH6_AM_N: now also L34.13 (DM_N); no longer L34.22 (AM_N)
- net ETH6_AM_P: now also L34.14 (DM_P); no longer L34.23 (AM_P)
- net ETH6_A_N: now also L34.12 (D_N); no longer L34.3 (A_N)
- net ETH6_A_P: now also L34.11 (D_P); no longer L34.2 (A_P)
- net ETH6_BM_N: now also L34.16 (CM_N); no longer L34.19 (BM_N)
- net ETH6_BM_P: now also L34.17 (CM_P); no longer L34.20 (BM_P)
- net ETH6_B_N: now also L34.9 (C_N); no longer L34.6 (B_N)
- net ETH6_B_P: now also L34.8 (C_P); no longer L34.5 (B_P)
- net ETH6_CM_N: now also L34.19 (BM_N); no longer L34.16 (CM_N)
- net ETH6_CM_P: now also L34.20 (BM_P); no longer L34.17 (CM_P)
- net ETH6_C_N: now also L34.6 (B_N); no longer L34.9 (C_N)
- net ETH6_C_P: now also L34.5 (B_P); no longer L34.8 (C_P)
- net ETH6_DM_N: now also L34.22 (AM_N); no longer L34.13 (DM_N)
- net ETH6_DM_P: now also L34.23 (AM_P); no longer L34.14 (DM_P)
- net ETH6_D_N: now also L34.3 (A_N); no longer L34.12 (D_N)
- net ETH6_D_P: now also L34.2 (A_P); no longer L34.11 (D_P)
- net ETH7_AM_N: now also L35.13 (DM_N); no longer L35.22 (AM_N)
- net ETH7_AM_P: now also L35.14 (DM_P); no longer L35.23 (AM_P)
- net ETH7_A_N: now also L35.12 (D_N); no longer L35.3 (A_N)
- net ETH7_A_P: now also L35.11 (D_P); no longer L35.2 (A_P)
- net ETH7_BM_N: now also L35.16 (CM_N); no longer L35.19 (BM_N)
- net ETH7_BM_P: now also L35.17 (CM_P); no longer L35.20 (BM_P)
- net ETH7_B_N: now also L35.9 (C_N); no longer L35.6 (B_N)
- net ETH7_B_P: now also L35.8 (C_P); no longer L35.5 (B_P)
- net ETH7_CM_N: now also L35.19 (BM_N); no longer L35.16 (CM_N)
- net ETH7_CM_P: now also L35.20 (BM_P); no longer L35.17 (CM_P)
- net ETH7_C_N: now also L35.6 (B_N); no longer L35.9 (C_N)
- net ETH7_C_P: now also L35.5 (B_P); no longer L35.8 (C_P)
- net ETH7_DM_N: now also L35.22 (AM_N); no longer L35.13 (DM_N)
- net ETH7_DM_P: now also L35.23 (AM_P); no longer L35.14 (DM_P)
- net ETH7_D_N: now also L35.3 (A_N); no longer L35.12 (D_N)
- net ETH7_D_P: now also L35.2 (A_P); no longer L35.11 (D_P)

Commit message: Continued initial layout, mostly on PHY indicator LEDs.
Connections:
- net LED_0_1: now also Q2.G2 (G); no longer Q3.G2 (G)
- net LED_0_2: now also Q3.G2 (G); no longer Q4.G1 (G)
- net LED_0_4: now also Q5.G2 (G); no longer Q7.G1 (G)
- net LED_0_6: now also Q6.G2 (G); no longer Q8.G1 (G)
- net LED_1_2: now also Q3.G1 (G); no longer Q2.G2 (G)
- net LED_1_3: now also Q4.G1 (G); no longer Q3.G1 (G)
- net LED_1_5: now also Q7.G1 (G); no longer Q5.G2 (G)
- net LED_1_7: now also Q8.G1 (G); no longer Q6.G2 (G)
- net at Q3.D2 (D): now also R72.2; no longer R71.2
- net at Q2.D2 (D): now also R71.2; no longer R59.2
- net at Q4.D1 (D): now also R61.2; no longer R72.2
- net at Q3.D1 (D): now also R59.2; no longer R61.2
- net at Q7.D1 (D): now also R122.2; no longer R139.2
- net at Q5.D2 (D): now also R139.2; no longer R122.2
- net at Q8.D1 (D): now also R126.2; no longer R141.2
- net at Q6.D2 (D): now also R141.2; no longer R126.2
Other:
- moved on the sheet: Q2B, Q3A, Q3B, Q4A, Q5B, Q6B, Q7A, Q8A
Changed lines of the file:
@@
 L special-azonenberg:SSM6N58NU_DUAL_NMOS Q3
 U 2 1 5B47B6FB
-P 11800 10550
-F 0 "Q3" H 11941 10656 60  0000 L CNN
-F 1 "SSM6N58NU" H 11941 10550 60  0000 L CNN
-F 2 "azonenberg_pcb:DFN_6_0.65MM_2x2MM_GDS" H 11800 10550 60  0001 C CNN
-F 3 "transistors/mos/*.*" H 11941 10444 60  0000 L CNN
-	2    11800 10550
+P 11850 15250
+F 0 "Q3" H 11991 15356 60  0000 L CNN
+F 1 "SSM6N58NU" H 11991 15250 60  0000 L CNN
+F 2 "azonenberg_pcb:DFN_6_0.65MM_2x2MM_GDS" H 11850 15250 60  0001 C CNN
+F 3 "transistors/mos/*.*" H 11991 15144 60  0000 L CNN
+	2    11850 15250
 	1    0    0    -1
 $EndComp
@@
 L special-azonenberg:SSM6N58NU_DUAL_NMOS Q2
 U 2 1 5B5CE7A7
-P 10300 15250
-F 0 "Q2" H 10441 15356 60  0000 L CNN
-F 1 "SSM6N58NU" H 10441 15250 60  0000 L CNN
-F 2 "azonenberg_pcb:DFN_6_0.65MM_2x2MM_GDS" H 10300 15250 60  0001 C CNN
-F 3 "transistors/mos/*.*" H 10441 15144 60  0000 L CNN
-	2    10300 15250
+P 11800 10550
+F 0 "Q2" H 11941 10656 60  0000 L CNN
+F 1 "SSM6N58NU" H 11941 10550 60  0000 L CNN
+F 2 "azonenberg_pcb:DFN_6_0.65MM_2x2MM_GDS" H 11800 10550 60  0001 C CNN
+F 3 "transistors/mos/*.*" H 11941 10444 60  0000 L CNN
+	2    11800 10550
 	1    0    0    -1
 $EndComp
@@
 L special-azonenberg:SSM6N58NU_DUAL_NMOS Q4
 U 1 1 5B5CE7BD
-P 11850 15250
-F 0 "Q4" H 11991 15356 60  0000 L CNN
-F 1 "SSM6N58NU" H 11991 15250 60  0000 L CNN
-F 2 "azonenberg_pcb:DFN_6_0.65MM_2x2MM_GDS" H 11850 15250 60  0001 C CNN
-F 3 "transistors/mos/*.*" H 11991 15144 60  0000 L CNN
-	1    11850 15250
+P 10300 20000
+F 0 "Q4" H 10441 20106 60  0000 L CNN
+F 1 "SSM6N58NU" H 10441 20000 60  0000 L CNN
+F 2 "azonenberg_pcb:DFN_6_0.65MM_2x2MM_GDS" H 10300 20000 60  0001 C CNN
+F 3 "transistors/mos/*.*" H 10441 19894 60  0000 L CNN
+	1    10300 20000
 	1    0    0    -1
 $EndComp
@@
 L special-azonenberg:SSM6N58NU_DUAL_NMOS Q3
 U 1 1 5B6DCDFE
-P 10300 20000
-F 0 "Q3" H 10441 20106 60  0000 L CNN
-F 1 "SSM6N58NU" H 10441 20000 60  0000 L CNN
-F 2 "azonenberg_pcb:DFN_6_0.65MM_2x2MM_GDS" H 10300 20000 60  0001 C CNN
-F 3 "transistors/mos/*.*" H 10441 19894 60  0000 L CNN
-	1    10300 20000
+P 10300 15250
+F 0 "Q3" H 10441 15356 60  0000 L CNN
+F 1 "SSM6N58NU" H 10441 15250 60  0000 L CNN
+F 2 "azonenberg_pcb:DFN_6_0.65MM_2x2MM_GDS" H 10300 15250 60  0001 C CNN
+F 3 "transistors/mos/*.*" H 10441 15144 60  0000 L CNN
+	1    10300 15250
 	1    0    0    -1
 $EndComp
@@
 L special-azonenberg:SSM6N58NU_DUAL_NMOS Q7
 U 1 1 5BB3FB5C
-P 23650 5800
-F 0 "Q7" H 23791 5906 60  0000 L CNN
-F 1 "SSM6N58NU" H 23791 5800 60  0000 L CNN
-F 2 "azonenberg_pcb:DFN_6_0.65MM_2x2MM_GDS" H 23650 5800 60  0001 C CNN
-F 3 "transistors/mos/*.*" H 23791 5694 60  0000 L CNN
-	1    23650 5800
+P 22100 10550
+F 0 "Q7" H 22241 10656 60  0000 L CNN
+F 1 "SSM6N58NU" H 22241 10550 60  0000 L CNN
+F 2 "azonenberg_pcb:DFN_6_0.65MM_2x2MM_GDS" H 22100 10550 60  0001 C CNN
+F 3 "transistors/mos/*.*" H 22241 10444 60  0000 L CNN
+	1    22100 10550
 	1    0    0    -1
 $EndComp
@@
 L special-azonenberg:SSM6N58NU_DUAL_NMOS Q5
 U 2 1 5BB3FD68
-P 22100 10550
-F 0 "Q5" H 22241 10656 60  0000 L CNN
-F 1 "SSM6N58NU" H 22241 10550 60  0000 L CNN
-F 2 "azonenberg_pcb:DFN_6_0.65MM_2x2MM_GDS" H 22100 10550 60  0001 C CNN
-F 3 "transistors/mos/*.*" H 22241 10444 60  0000 L CNN
-	2    22100 10550
+P 23650 5800
+F 0 "Q5" H 23791 5906 60  0000 L CNN
+F 1 "SSM6N58NU" H 23791 5800 60  0000 L CNN
+F 2 "azonenberg_pcb:DFN_6_0.65MM_2x2MM_GDS" H 23650 5800 60  0001 C CNN
+F 3 "transistors/mos/*.*" H 23791 5694 60  0000 L CNN
+	2    23650 5800
 	1    0    0    -1
 $EndComp
@@
 L special-azonenberg:SSM6N58NU_DUAL_NMOS Q8
 U 1 1 5BB3FFB8
-P 23700 15250
-F 0 "Q8" H 23841 15356 60  0000 L CNN
-F 1 "SSM6N58NU" H 23841 15250 60  0000 L CNN
-F 2 "azonenberg_pcb:DFN_6_0.65MM_2x2MM_GDS" H 23700 15250 60  0001 C CNN
-F 3 "transistors/mos/*.*" H 23841 15144 60  0000 L CNN
-	1    23700 15250
+P 22150 20000
+F 0 "Q8" H 22291 20106 60  0000 L CNN
+F 1 "SSM6N58NU" H 22291 20000 60  0000 L CNN
+F 2 "azonenberg_pcb:DFN_6_0.65MM_2x2MM_GDS" H 22150 20000 60  0001 C CNN
+F 3 "transistors/mos/*.*" H 22291 19894 60  0000 L CNN
+	1    22150 20000
 	1    0    0    -1
 $EndComp
@@
 L special-azonenberg:SSM6N58NU_DUAL_NMOS Q6
 U 2 1 5BB401DD
-P 22150 20000
-F 0 "Q6" H 22291 20106 60  0000 L CNN
-F 1 "SSM6N58NU" H 22291 20000 60  0000 L CNN
-F 2 "azonenberg_pcb:DFN_6_0.65MM_2x2MM_GDS" H 22150 20000 60  0001 C CNN
-F 3 "transistors/mos/*.*" H 22291 19894 60  0000 L CNN
-	2    22150 20000
+P 23700 15250
+F 0 "Q6" H 23841 15356 60  0000 L CNN
+F 1 "SSM6N58NU" H 23841 15250 60  0000 L CNN
+F 2 "azonenberg_pcb:DFN_6_0.65MM_2x2MM_GDS" H 23700 15250 60  0001 C CNN
+F 3 "transistors/mos/*.*" H 23841 15144 60  0000 L CNN
+	2    23700 15250
 	1    0    0    -1
 $EndComp
